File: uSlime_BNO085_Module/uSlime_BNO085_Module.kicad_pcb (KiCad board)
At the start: 2 copper layers, 16.7 x 12.8 mm, 16 parts, among them CN1 X1502WR-05K-N0SN, J1 Conn_01x05, U1 BNO085

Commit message: Connect pin 26 to GND
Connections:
- U1 pad 26: unconnected-(U1-XOUT32/CLKSEL1-Pad26) -> GND
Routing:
- net GND: track 16.5 -> 17.9 mm

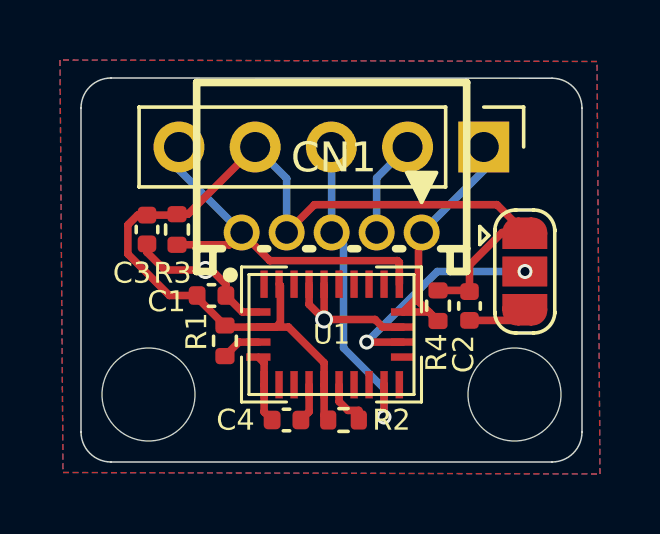
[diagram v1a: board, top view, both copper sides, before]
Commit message: Add dingyifei to PCB ref
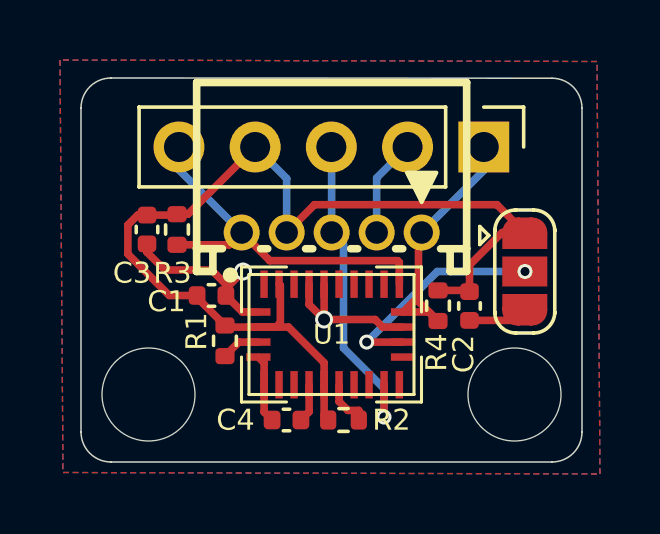
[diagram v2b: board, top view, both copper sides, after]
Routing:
- net GND: track 17.9 -> 18.9 mm
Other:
- board text added: "dingyifei"

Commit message: Modify PCB to add resistors to pins 14, 15, 16
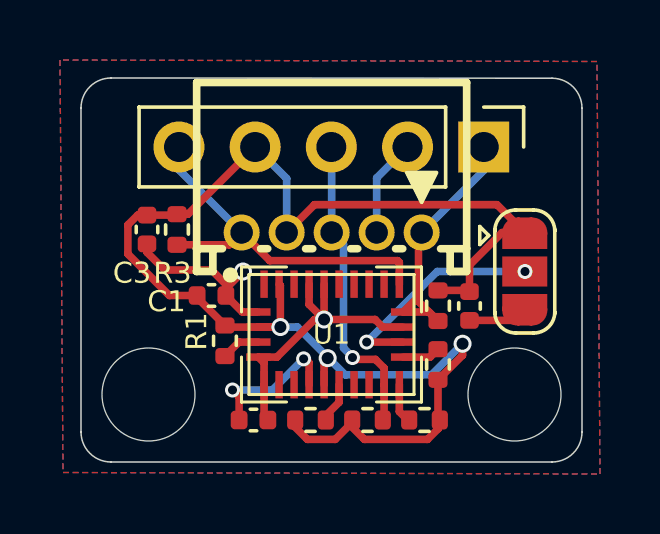
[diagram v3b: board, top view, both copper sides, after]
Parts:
- added R5: 10k, Resistor_SMD:R_0402_1005Metric, F.Cu at (110.2, 100.8)
- added R6: 2.2k, Resistor_SMD:R_0402_1005Metric, F.Cu at (112.1, 100.8)
- added R7: 2.2k, Resistor_SMD:R_0402_1005Metric, F.Cu at (112.5, 98.9)
- moved R2 1.10 mm to (108.3, 100.8)
- moved C4 1.10 mm to (106.4, 100.8), turned to 180 degrees
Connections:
- U1 pad 15: unconnected-(U1-ENV_SCL-Pad15) -> Net-(U1-ENV_SCL)
- U1 pad 16: unconnected-(U1-ENV_SDA-Pad16) -> Net-(U1-ENV_SDA)
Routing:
- net +3.3V: track 34.7 -> 47.8 mm, vias 0 -> 3
- net Net-(U1-CAP): track 1.29 -> 4.86 mm, vias 0 -> 2
- net GND: track 18.9 -> 21.6 mm
- net Net-(U1-ENV_SCL): track 0.00 -> 1.29 mm
- net Net-(U1-ENV_SDA): track 0.00 -> 1.27 mm
- net BNO_INT2: track 10.8 -> 10.3 mm

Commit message: v1.0.0 - Use 1206 LED, add resistor pack suggestion
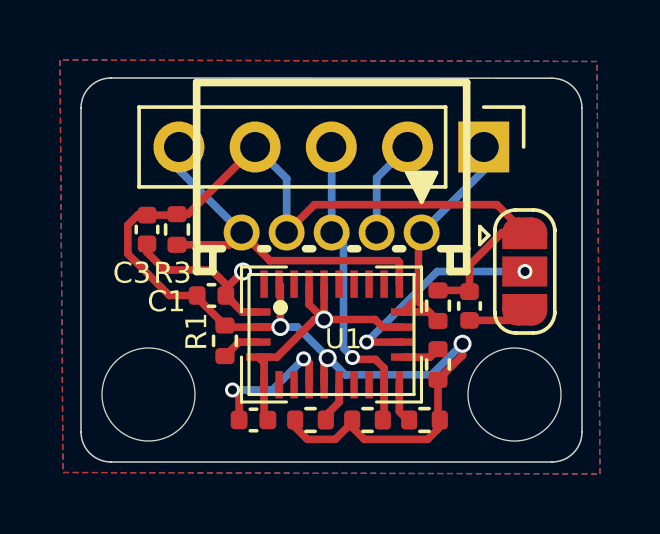
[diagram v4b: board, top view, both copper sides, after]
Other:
- board text added: "v1.0.0"
- board text removed: "v0.0.5a"

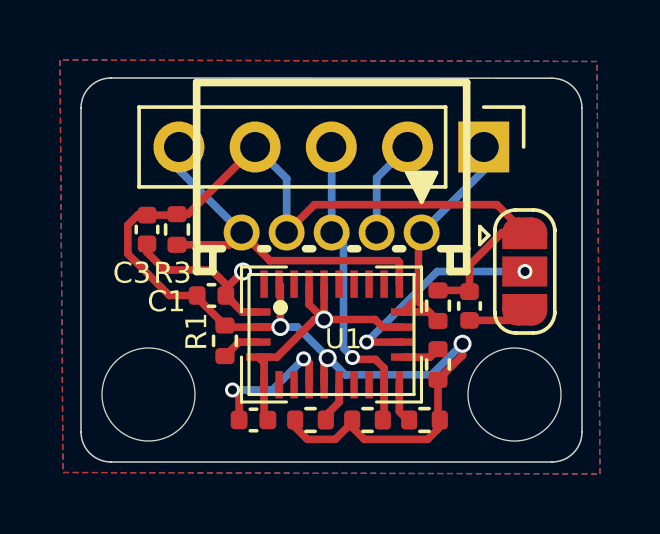
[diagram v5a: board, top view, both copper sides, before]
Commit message: Export mainboard PCB for JLC ident placement
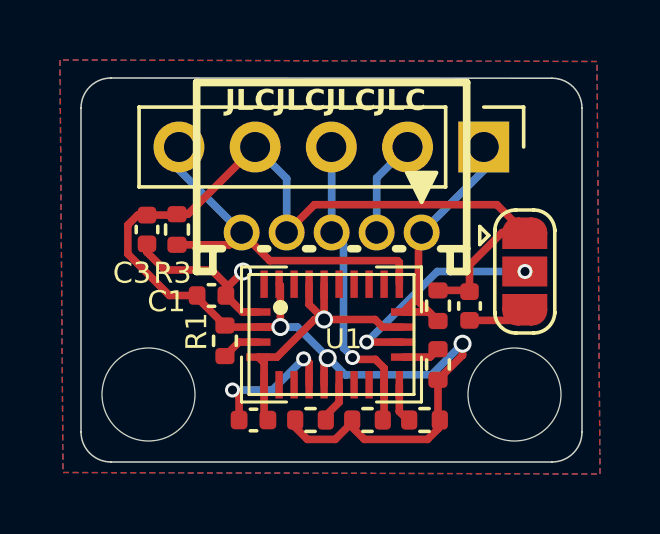
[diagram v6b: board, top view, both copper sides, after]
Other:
- board text added: "JLCJLCJLCJLC"
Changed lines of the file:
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@@
+		)
+	)
+	(gr_text "JLCJLCJLCJLC"
+		(at 108.8 90.5 0)
+		(layer "F.SilkS")
+		(effects
+			(font
+				(size 0.7 0.7)
+				(thickness 0.175)
+				(bold yes)
+			)
+			(justify bottom)
 		)
 	)
